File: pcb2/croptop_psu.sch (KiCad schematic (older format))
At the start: 41 parts

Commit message: Added USB port control
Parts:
- added C? (x2): 100uF, Capacitor_SMD:CP_Elec_6.3x7.7, symbol Device:CP1
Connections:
- wire segments 148 -> 154
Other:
- moved on the sheet: C?, D?, J?, L?, R?, TP?, U?

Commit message: Schematic near completion
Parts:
- removed C?: 10uF, Capacitor_SMD:C_0805_2012Metric, symbol Device:C
- removed C?: 560pF, Capacitor_SMD:C_0603_1608Metric, symbol Device:C
- removed D?: LED, LED_SMD:LED_0805_2012Metric, symbol Device:LED
- removed R?: 100, Resistor_SMD:R_0402_1005Metric, symbol Device:R
- removed R?: 60, Resistor_SMD:R_0402_1005Metric, symbol Device:R
- removed U?: MIC23050, Package_DFN_QFN:DFN-8-1EP_2x2mm_P0.45mm_EP0.64x1.38mm, symbol CropTop:MIC23050
- added C?: 0.1uF, Capacitor_SMD:C_0402_1005Metric, symbol Device:C
- added D? (x2): LED, LED_SMD:LED_0805_2012Metric, symbol Device:LED
- added F?: Polyfuse, symbol Device:Polyfuse
- added R?: 60, Resistor_SMD:R_0402_1005Metric, symbol Device:R
- added R?: 0, Resistor_SMD:R_0402_1005Metric, symbol Device:R
- added R?: 220, Resistor_SMD:R_0402_1005Metric, symbol Device:R
- added U?: TPS62131, Package_DFN_QFN:QFN-16-1EP_3x3mm_P0.5mm_EP1.8x1.8mm, symbol CropTop:TPS62131
- C? (x3): footprint Capacitor_SMD:C_0805_2012Metric -> Capacitor_SMD:C_0402_1005Metric
- C?: value 1uF -> 10uF
- J?: value 5V USB -> 10118193-0001LF
- L?: value 1uH -> 2.2uH; footprint Inductor_SMD:L_0805_2012Metric -> (none); Note (none) -> SRN8040-2R2Y
- R?: value R -> 2k; footprint (none) -> Resistor_SMD:R_0402_1005Metric
- R?: value R -> 100; footprint (none) -> Resistor_SMD:R_0402_1005Metric
- R?: value R -> 220; footprint (none) -> Resistor_SMD:R_0402_1005Metric
- R?: footprint Resistor_SMD:R_0603_1608Metric -> Resistor_SMD:R_0402_1005Metric
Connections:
- wire segments 154 -> 172
- no-connect marks 4 -> 3
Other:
- note added: "(50ms Soft Start)"
- note added: "Low Noise 5V Plane"
- note removed: "5V"
- moved on the sheet: C?, D?, J?, L?, R?, TP?

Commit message: Added pmod
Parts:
- removed C? (x4): 0.1uF, Capacitor_SMD:C_0402_1005Metric, symbol Device:C
- removed C? (x3): 1uF, Capacitor_SMD:C_0402_1005Metric, symbol Device:C
- removed C?: 470pF, Capacitor_SMD:C_0402_1005Metric, symbol Device:C
- removed D?: 3SMAJ5935B, croptop:DO-214AC, symbol Device:D_Zener
- removed D?: LED, LED_SMD:LED_0805_2012Metric, symbol Device:LED
- removed F?: Polyfuse, symbol Device:Polyfuse
- removed R?: 60, Resistor_SMD:R_0402_1005Metric, symbol Device:R
- removed U?: FAN5333BSX, Package_TO_SOT_SMD:SOT-23-5, symbol CropTop:FAN5333BSX
- removed U?: TC1014, Package_TO_SOT_SMD:SOT-23-5, symbol CropTop:TC1014
- added C? (x6): 10uF, Capacitor_SMD:C_0402_1005Metric, symbol Device:C
- added C? (x2): 0.1uF, Capacitor_SMD:C_0402_1005Metric, symbol Device:C
- added D?: LTSTC171GKT, LED_SMD:LED_0805_2012Metric, symbol Device:LED
- added R? (x2): 220, Resistor_SMD:R_0402_1005Metric, symbol Device:R
- added R? (x2): 100, Resistor_SMD:R_0402_1005Metric, symbol Device:R
- added TP?: TestPoint, symbol Connector:TestPoint
- added U?: TPS61169, symbol CropTop:TPS61169
- added U?: TPS70950, symbol CropTop:TPS70950
- D?: value BAT42W -> NSR0240HT1G
- D? (x4): value LED -> LTSTC171GKT
- L?: MPN (none) -> SRN8040-2R2Y; Note SRN8040-2R2Y -> (none)
- L?: value 10uH -> 4.7uH; MPN (none) -> SRN6045TA-4R7M
- R?: value 2k -> 220
- R?: value 2.2 -> 1.1; MPN (none) -> RC1005F1R1CS
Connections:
- wire segments 172 -> 180
- no-connect marks 3 -> 4
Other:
- note added: "(3s9p)"
- note added: "(approx. 9.6V)"
- note added: "Individual LEDs:\n3.2V Forward Voltage\n20mA Typical / 25mA Max\n\nTotal:\n9.6V Forward Voltage\n180mA Typical / 225mA Max"
- note added: "RC1005F1R1CS"
- note added: "SRN6045TA-4R7M"
- note added: "SRN8040-2R2Y"
- note removed: "(approx. 25.6V)"
- moved on the sheet: C?, D?, J?, L?, R?, TP?, U?

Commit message: pwm
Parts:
- R13, R17, R18, R19, R21: renamed from R?; value 220 -> 220Ω
- R14, R15, R20: renamed from R?; value 100 -> 100Ω
- R16: renamed from R?; value 1.1 -> 1.1Ω
- R22: renamed from R?; value 0 -> 0Ω
- gave numbers to parts that had none: 37

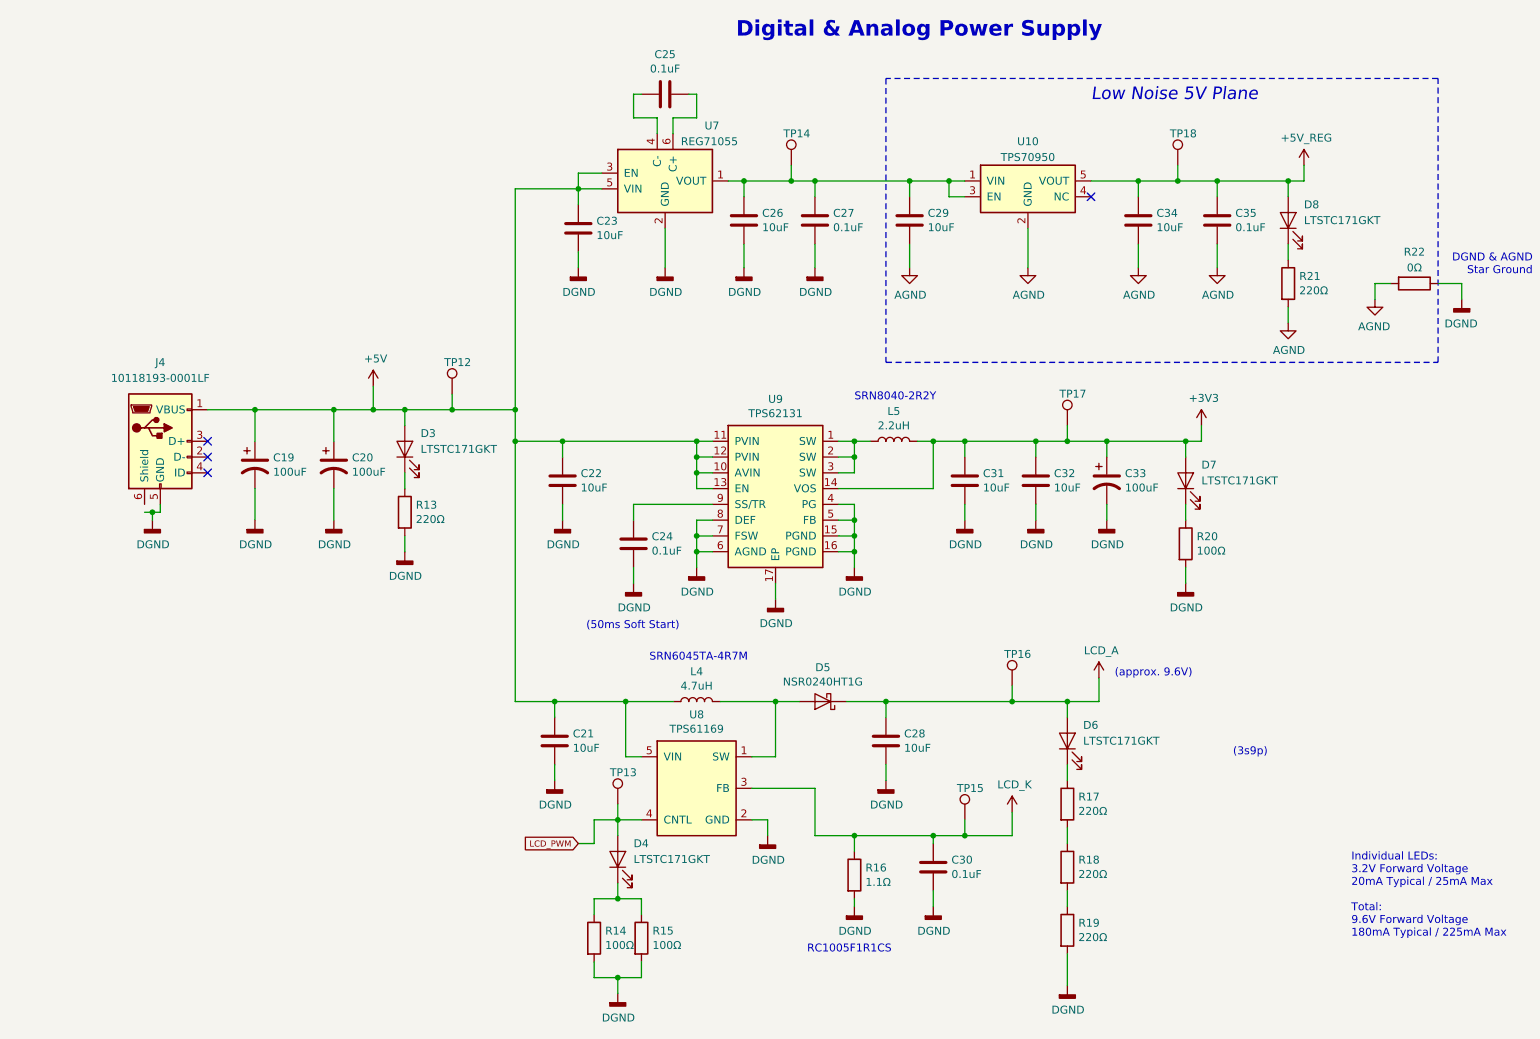
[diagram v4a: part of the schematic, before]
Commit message: Added TVS diodes
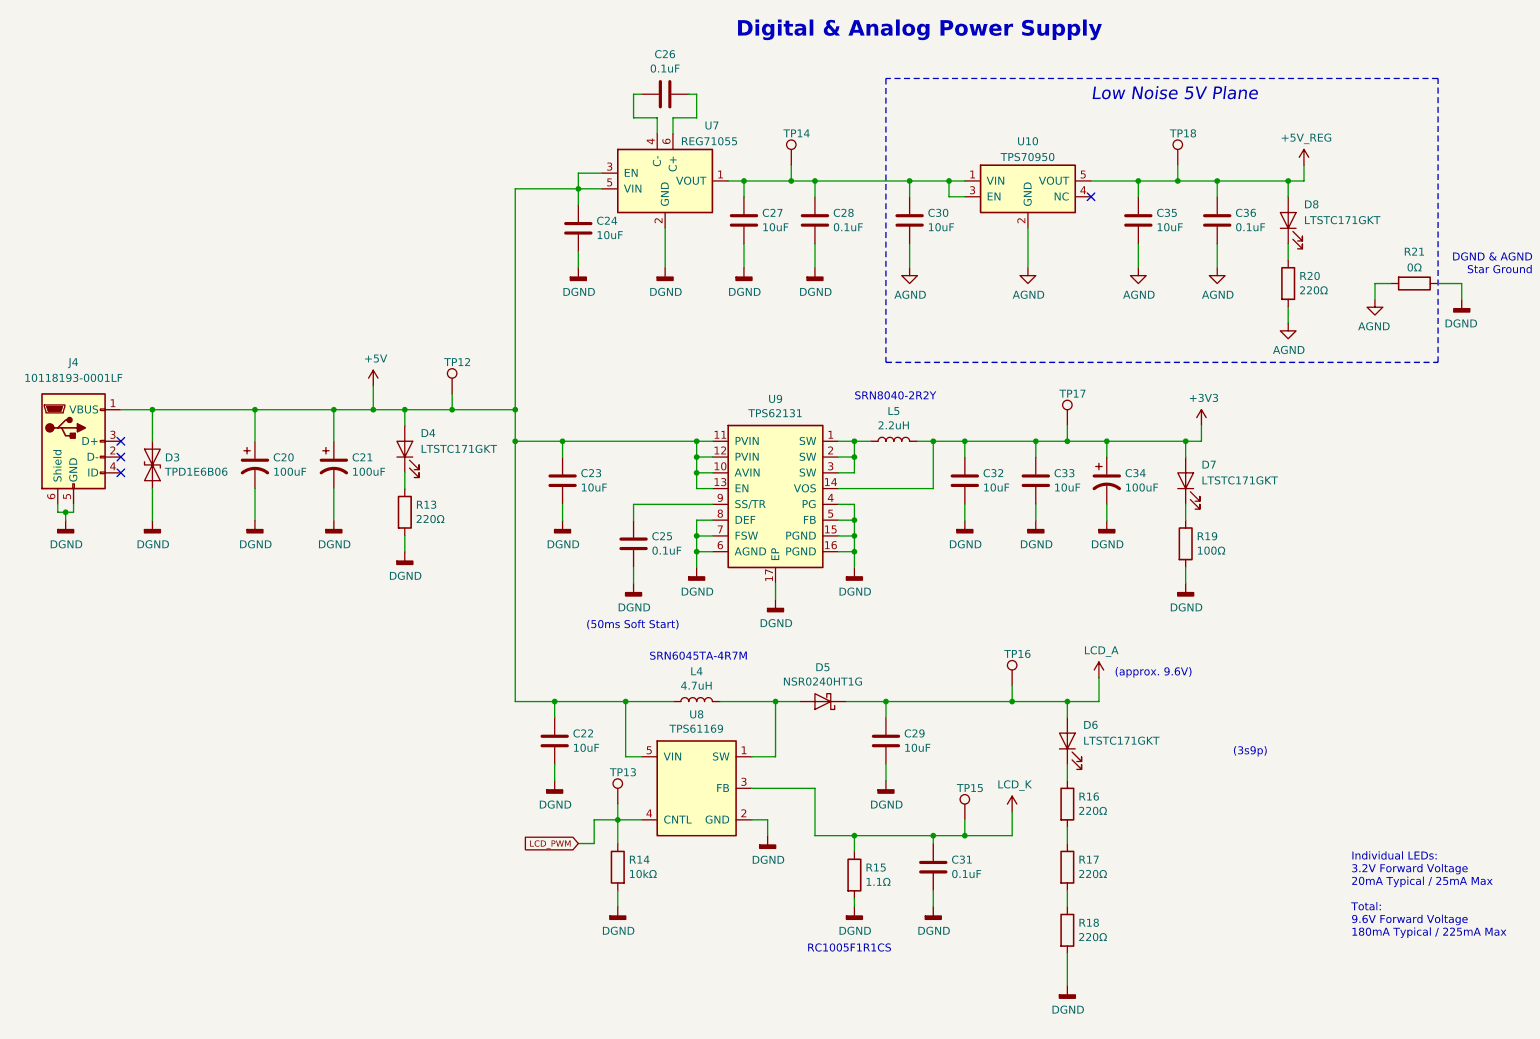
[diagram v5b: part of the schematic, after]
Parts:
- removed D4: LTSTC171GKT, LED_SMD:LED_0805_2012Metric, symbol Device:LED
- removed R15: 100Ω, Resistor_SMD:R_0402_1005Metric, symbol Device:R
- added D3: TPD1E6B06, symbol Device:D_TVS
- R14: value 100Ω -> 10kΩ
- renumbered C19 to C20, C20 to C21, C21 to C22, C22 to C23, C23 to C24, C24 to C25, C25 to C26, C26 to C27, C27 to C28, C28 to C29, C29 to C30, C30 to C31, C31 to C32, C32 to C33, C33 to C34, C34 to C35, C35 to C36, D3 to D4, R16 to R15, R17 to R16, R18 to R17, R19 to R18, R20 to R19, R21 to R20, R22 to R21
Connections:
- net +5V: now also D3.1 (A1)
- net DGND: now also J4.6 (Shield), D3.2 (A2)
- net LCD_PWM: now also R14.1
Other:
- moved on the sheet: J4

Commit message: Updated pin out
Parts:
- removed C28: 0.1uF, Capacitor_SMD:C_0402_1005Metric, symbol Device:C
- added C? (x5): 10uF, Capacitor_SMD:C_0402_1005Metric, symbol Device:C
- added C? (x11): 0.1uF, Capacitor_SMD:C_0402_1005Metric, symbol Device:C
- added C? (x2): 26pF, Capacitor_SMD:C_0402_1005Metric, symbol Device:C
- added D?: LTSTC171GKT, LED_SMD:LED_0805_2012Metric, symbol Device:LED
- added FID? (x2): Fiducial, Fiducial:Fiducial_1mm_Dia_2.54mm_Outer_CopperTop, symbol CropTop:FIDUCIAL
- added H? (x4): 4mm Mounting Hole, MountingHole:MountingHole_4mm_Pad, symbol Mechanical:MountingHole
- added J?: 68000-206HLF, symbol Connector_Generic:Conn_01x06
- added J?: USB-A1HSW6, croptop:USB_A_Assmann_Horizontal, symbol Connector:USB_A
- added L?: BKP1005HS121, symbol Device:L_Core_Ferrite
- added R? (x7): 10k, Resistor_SMD:R_0402_1005Metric, symbol Device:R
- added R?: 100, Resistor_SMD:R_0402_1005Metric, symbol Device:R
- added SW?: SW_Push, symbol Switch:SW_Push
- added TP? (x4): TestPoint, symbol Connector:TestPoint
- added U? (x2): PIC32MX795F512L, digikey-footprints:TQFP-100_12x12mm, symbol CropTop:PIC32MX795F512L-80I_PT_0
- added U?: TPD4E1U06, symbol CropTop:TPD4E1U06
- added U?: AP22802AW5, symbol CropTop:AP22802AW5
- added Y?: ABLS-8.000MHZ-B4-T, croptop:ABLS_OX, symbol Device:Crystal
- R13, R16, R17, R18, R20: value 220Ω -> 220
- R14: value 10kΩ -> 10k
- R15: value 1.1Ω -> 1.1
- R19: value 100Ω -> 100
- R21: value 0Ω -> 0
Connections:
- net +3V3: now also C?.1, C?.1, C?.1, C?.1, C?.1, C?.1, C?.1, C?.1, C?.1, J?.2 (Pin_2), L?.1, R?.1, R?.1, R?.1, R?.1, R?.1, U?.16 (VDD), U?.2 (VDD), U?.37 (VDD), U?.4 (EN), U?.46 (VDD), U?.55 (VUSB3V3), U?.62 (VDD), U?.86 (VDD)
- net DGND: now also C?.2, C?.2, C?.2, C?.2, C?.2, C?.2, C?.2, C?.2, C?.2, C?.2, C?.2, C?.2, C?.2, C?.2, C?.2, C?.2, C?.2, C?.2, J?.3 (Pin_3), J?.4 (GND), J?.5 (Shield), R?.2, R?.2, R?.2, SW?.2, U?.15 (VSS), U?.2 (GND), U?.2 (GND), U?.31 (AVSS), U?.36 (VSS), U?.45 (VSS), U?.65 (VSS), U?.75 (VSS)
- net LCD_PWM renamed GCD_PWM
- new net: C?.1, U?.63 (OSC1), Y?.1
- new net: C?.1, U?.64 (OSC2), Y?.2
- new net: C?.1, C?.1, L?.2, U?.30 (AVDD)
- new net: C?.1, U?.85 (VCAP/VDDCORE)
- new net: C?.1, C?.1, D?.2 (A), J?.1 (VBUS), TP?.1, U?.1 (OUT)
- new net: J?.2 (D-), U?.3 (D2+)
- new net: J?.3 (D+), U?.4 (D2-)
- new net: C?.1, U?.5 (IN)
- new net: D?.1 (K), R?.1
- new net: R?.2, TP?.1, U?.3 (FLG)
- new net CONFIG_ADC: R?.1, R?.2, TP?.1
- new net ONBRD_SCL: R?.2, U?.58 (SCL2)
- new net ONBRD_SDA: R?.2, U?.59 (SDA2)
- new net PKT_MCLR: C?.1, J?.1 (Pin_1), R?.2, SW?.1, TP?.1
- new net PKT_PGEC: J?.5 (Pin_5)
- new net PKT_PGED: J?.4 (Pin_4)
- new net USB_PWR_EN: U?.54 (VBUS)
- no-connect marks 4 -> 11
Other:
- note added: "Bulk"
- note added: "Cart: 10K\nPusher: 10K\nStabber: 2K"
- note added: "Cart: 2K\nPusher: 10K\nStabber: 10K"
- note added: "MCU Reset"
- note added: "Mounting Holes & Fiducials"
- note added: "No Pin"
- note added: "PIC32 Microcontroller"
- note added: "PICKit3 Programming Header"
- note added: "Pin 15"
- note added: "Pin 16"
- note added: "Pin 2"
- note added: "Pin 30"
- note added: "Pin 31\n"
- note added: "Pin 36"
- note added: "Pin 37"
- note added: "Pin 45"
- note added: "Pin 46"
- note added: "Pin 62"
- note added: "Pin 65"
- note added: "Pin 75"
- note added: "Software Config Divider"
- note removed: "(3s9p)"
- moved on the sheet: C20, C21, C22, C23, C24, C25, C26, C27, C29, C30, C31, C32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
